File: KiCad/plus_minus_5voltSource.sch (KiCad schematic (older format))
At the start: 15 parts, among them P1 CONN_01X03, SW1 SW_Push, U1 LM7805_TO220, U2 7660, U3 LM79L05_TO92

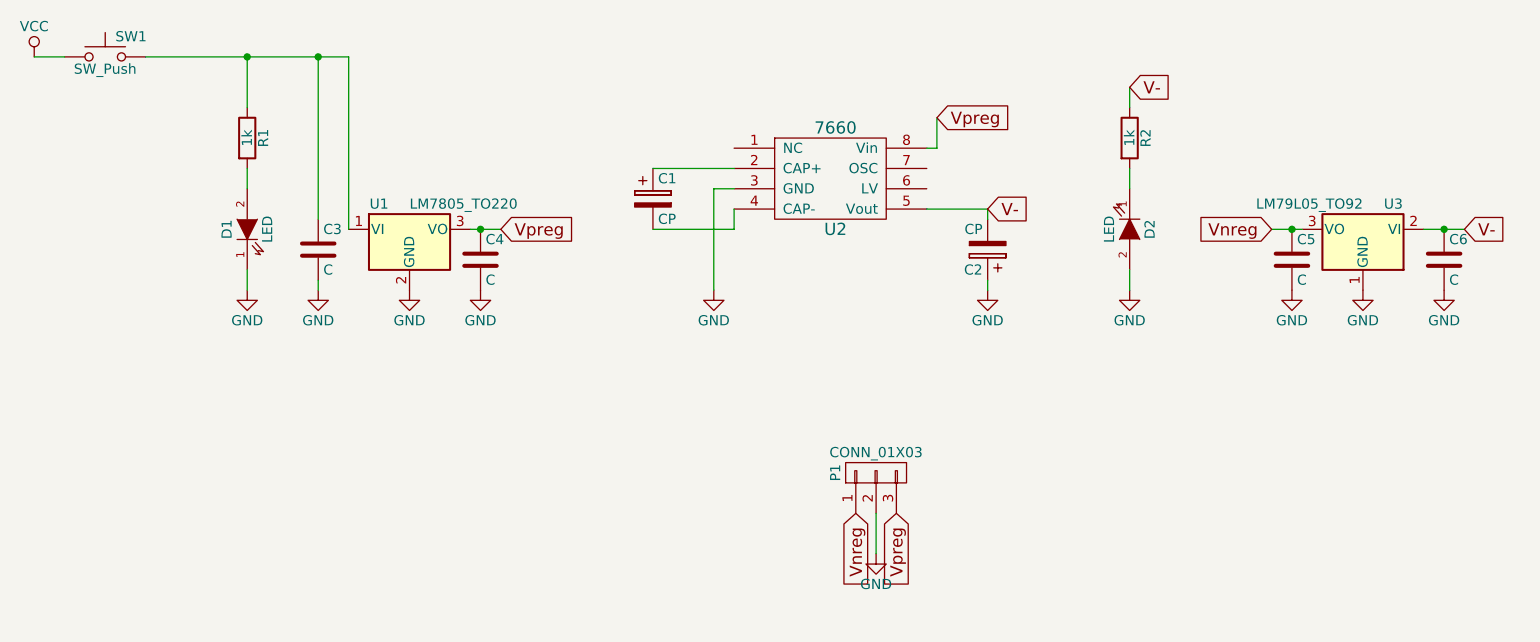
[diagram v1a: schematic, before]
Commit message: Finalized schematic by adding the usb connector for power and ground.
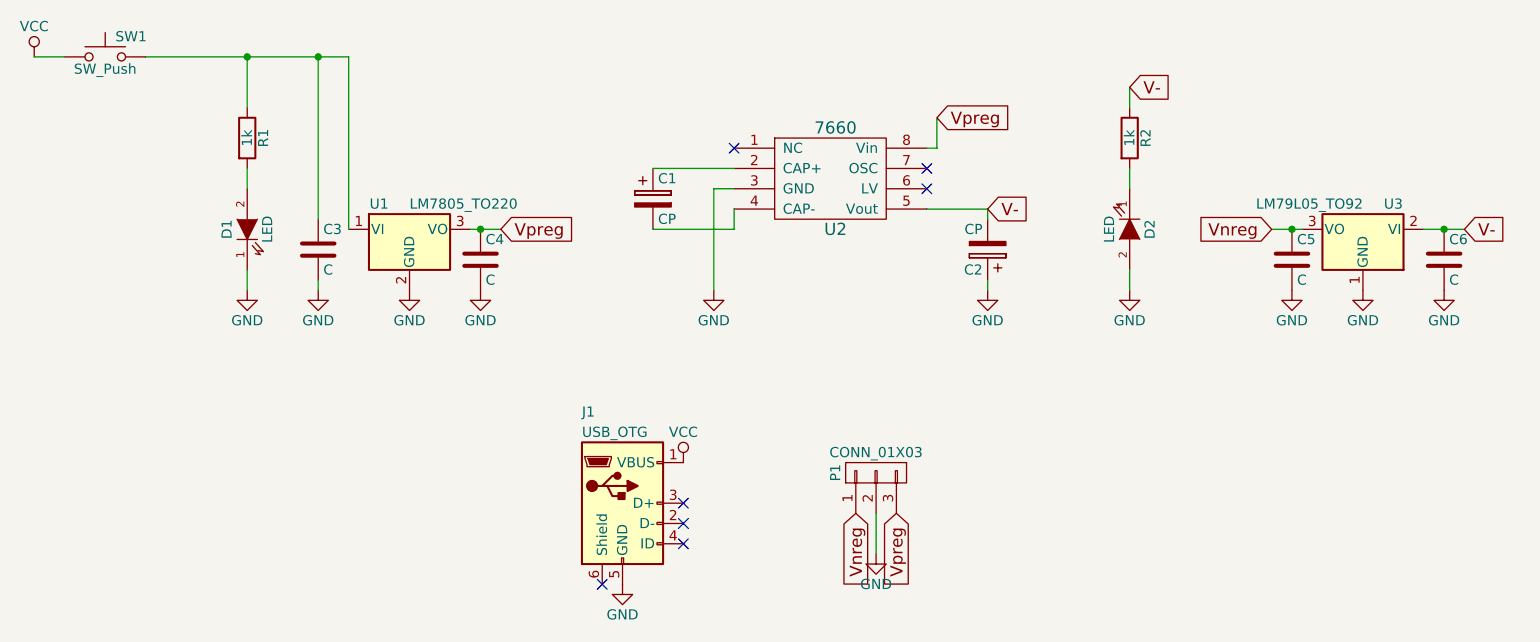
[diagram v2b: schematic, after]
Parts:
- added J1: USB_OTG, symbol USB_OTG
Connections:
- net GND: now also J1.5 (GND)
- net VCC: now also J1.1 (VBUS)
- no-connect marks 0 -> 7
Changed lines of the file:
@@
 	5550 3550 5150 3550
 $Comp
-L GND #PWR6
+L GND #PWR8
 U 1 1 55A2DE47
 P 5450 3850
-F 0 "#PWR6" H 5450 3600 50  0001 C CNN
+F 0 "#PWR8" H 5450 3600 50  0001 C CNN
 F 1 "GND" H 5450 3700 50  0000 C CNN
 F 2 "" H 5450 3850 60  0000 C CNN
@@
 	6800 3450 6500 3450
 $Comp
-L GND #PWR8
+L GND #PWR10
 U 1 1 55A2DF2E
 P 6800 3850
-F 0 "#PWR8" H 6800 3600 50  0001 C CNN
+F 0 "#PWR10" H 6800 3600 50  0001 C CNN
 F 1 "GND" H 6800 3700 50  0000 C CNN
 F 2 "" H 6800 3850 60  0000 C CNN
@@
 V-
 $Comp
-L GND #PWR7
+L GND #PWR9
 U 1 1 55A2E0F0
 P 6250 5150
-F 0 "#PWR7" H 6250 4900 50  0001 C CNN
+F 0 "#PWR9" H 6250 4900 50  0001 C CNN
 F 1 "GND" H 6250 5000 50  0000 C CNN
 F 2 "" H 6250 5150 60  0000 C CNN
@@
 $EndComp
 $Comp
-L GND #PWR9
+L GND #PWR11
 U 1 1 5796D7C9
 P 7500 3850
-F 0 "#PWR9" H 7500 3600 50  0001 C CNN
+F 0 "#PWR11" H 7500 3600 50  0001 C CNN
 F 1 "GND" H 7500 3700 50  0000 C CNN
 F 2 "" H 7500 3850 60  0000 C CNN
@@
 $EndComp
 $Comp
-L GND #PWR11
+L GND #PWR13
 U 1 1 5A2F6815
 P 8650 3850
-F 0 "#PWR11" H 8650 3600 50  0001 C CNN
+F 0 "#PWR13" H 8650 3600 50  0001 C CNN
 F 1 "GND" H 8650 3700 50  0000 C CNN
 F 2 "" H 8650 3850 60  0000 C CNN
@@
 Connection ~ 8300 3550
 $Comp
-L GND #PWR10
+L GND #PWR12
 U 1 1 5A2F7A77
 P 8300 3850
-F 0 "#PWR10" H 8300 3600 50  0001 C CNN
+F 0 "#PWR12" H 8300 3600 50  0001 C CNN
 F 1 "GND" H 8300 3700 50  0000 C CNN
 F 2 "" H 8300 3850 60  0000 C CNN
@@
 $EndComp
 $Comp
-L GND #PWR12
+L GND #PWR14
 U 1 1 5A2F7AAF
 P 9050 3850
-F 0 "#PWR12" H 9050 3600 50  0001 C CNN
+F 0 "#PWR14" H 9050 3600 50  0001 C CNN
 F 1 "GND" H 9050 3700 50  0000 C CNN
 F 2 "" H 9050 3850 60  0000 C CNN
@@
 	3500 3500 3500 2700
 Connection ~ 3500 2700
+$Comp
+L USB_OTG J1
+U 1 1 5A30A371
+P 5000 4900
+F 0 "J1" H 4800 5350 50  0000 L CNN
+F 1 "USB_OTG" H 4800 5250 50  0000 L CNN
+F 2 "" H 5150 4850 50  0001 C CNN
+F 3 "" H 5150 4850 50  0001 C CNN
+	1    5000 4900
+	1    0    0    -1
+$EndComp
+$Comp
+L GND #PWR6
+U 1 1 5A30A705
+P 5000 5300
+F 0 "#PWR6" H 5000 5050 50  0001 C CNN
+F 1 "GND" H 5000 5150 50  0000 C CNN
+F 2 "" H 5000 5300 60  0000 C CNN
+F 3 "" H 5000 5300 60  0000 C CNN
+	1    5000 5300
+	1    0    0    -1
+$EndComp
+$Comp
+L VCC #PWR7
+U 1 1 5A30A740
+P 5300 4700
+F 0 "#PWR7" H 5300 4550 50  0001 C CNN
+F 1 "VCC" H 5300 4850 50  0000 C CNN
+F 2 "" H 5300 4700 60  0000 C CNN
+F 3 "" H 5300 4700 60  0000 C CNN
+	1    5300 4700
+	1    0    0    -1
+$EndComp
+NoConn ~ 5300 4900
+NoConn ~ 5300 5000
+NoConn ~ 5300 5100
+NoConn ~ 4900 5300
+NoConn ~ 6500 3250
+NoConn ~ 6500 3350
+NoConn ~ 5550 3150
 $EndSCHEMATC

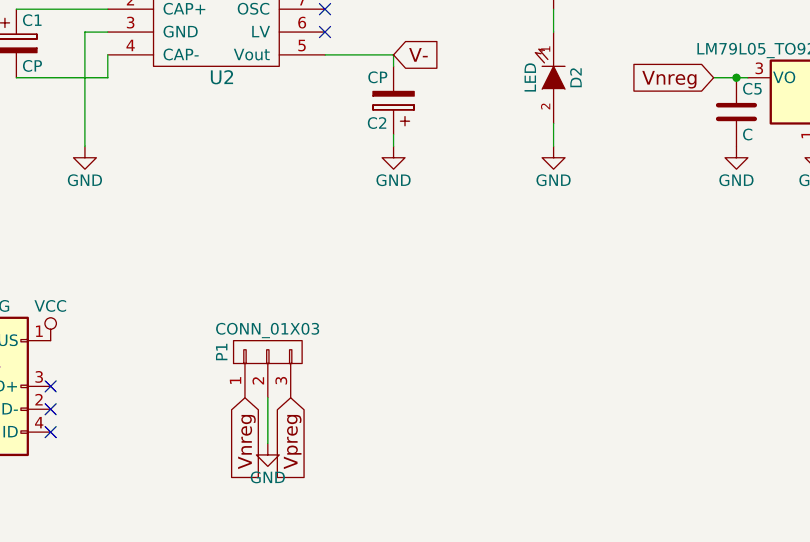
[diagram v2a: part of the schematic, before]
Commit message: Formatted BOM.
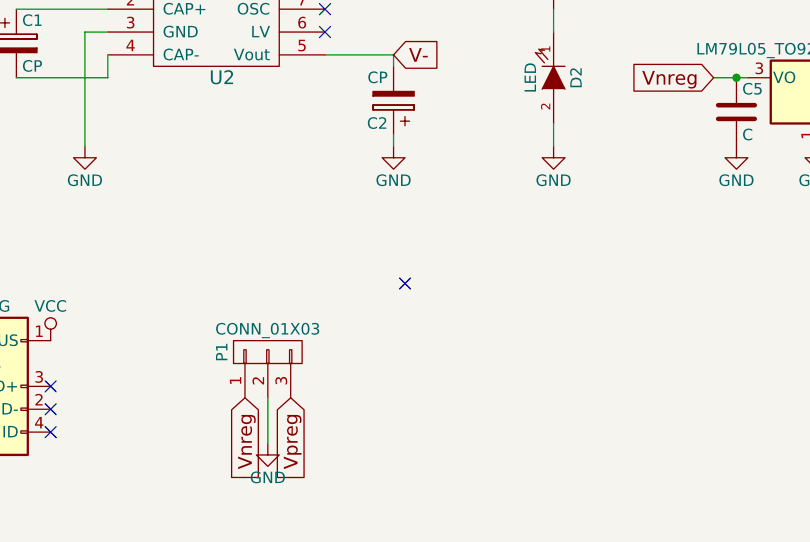
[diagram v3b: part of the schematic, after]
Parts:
- C1, C2: footprint Capacitors_ThroughHole:C_Radial_D5_L6_P2.5 -> Capacitors_ThroughHole:CP_Radial_D5.0mm_P2.50mm
- C3, C4, C5, C6: footprint (none) -> Capacitors_ThroughHole:C_Disc_D3.0mm_W2.0mm_P2.50mm
- D1, D2: footprint LEDs:LED_0805 -> LEDs:LED_D3.0mm
- J1: footprint (none) -> Connect:USB_Micro-B
- P1: footprint Pin_Headers:Pin_Header_Angled_1x03 -> Pin_Headers:Pin_Header_Angled_1x03_Pitch2.54mm
- R1, R2: footprint Resistors_SMD:R_0805_HandSoldering -> Resistors_ThroughHole:R_Axial_DIN0204_L3.6mm_D1.6mm_P5.08mm_Vertical
- SW1: footprint (none) -> Buttons_Switches_ThroughHole:SW_PUSH_6mm
- U1: footprint TO_SOT_Packages_THT:TO-220_Vertical -> TO_SOT_Packages_THT:TO-92_Inline_Narrow_Oval
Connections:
- no-connect marks 7 -> 8
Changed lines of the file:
@@
 F 0 "C1" H 5175 3500 50  0000 L CNN
 F 1 "CP" H 5175 3300 50  0000 L CNN
-F 2 "Capacitors_ThroughHole:C_Radial_D5_L6_P2.5" H 5188 3250 30  0001 C CNN
+F 2 "Capacitors_ThroughHole:CP_Radial_D5.0mm_P2.50mm" H 5188 3250 30  0001 C CNN
 F 3 "" H 5150 3400 60  0000 C CNN
 	1    5150 3400
@@
 F 0 "C2" H 6825 3750 50  0000 L CNN
 F 1 "CP" H 6825 3550 50  0000 L CNN
-F 2 "Capacitors_ThroughHole:C_Radial_D5_L6_P2.5" H 6838 3500 30  0001 C CNN
+F 2 "Capacitors_ThroughHole:CP_Radial_D5.0mm_P2.50mm" H 6838 3500 30  0001 C CNN
 F 3 "" H 6800 3650 60  0000 C CNN
 	1    6800 3650
@@
 	5550 3550 5150 3550
 $Comp
-L GND #PWR8
+L GND #PWR01
 U 1 1 55A2DE47
 P 5450 3850
-F 0 "#PWR8" H 5450 3600 50  0001 C CNN
+F 0 "#PWR01" H 5450 3600 50  0001 C CNN
 F 1 "GND" H 5450 3700 50  0000 C CNN
 F 2 "" H 5450 3850 60  0000 C CNN
@@
 	6800 3450 6500 3450
 $Comp
-L GND #PWR10
+L GND #PWR02
 U 1 1 55A2DF2E
 P 6800 3850
-F 0 "#PWR10" H 6800 3600 50  0001 C CNN
+F 0 "#PWR02" H 6800 3600 50  0001 C CNN
 F 1 "GND" H 6800 3700 50  0000 C CNN
 F 2 "" H 6800 3850 60  0000 C CNN
@@
 V-
 $Comp
-L GND #PWR9
+L GND #PWR03
 U 1 1 55A2E0F0
 P 6250 5150
-F 0 "#PWR9" H 6250 4900 50  0001 C CNN
+F 0 "#PWR03" H 6250 4900 50  0001 C CNN
 F 1 "GND" H 6250 5000 50  0000 C CNN
 F 2 "" H 6250 5150 60  0000 C CNN
@@
 F 0 "D1" H 3150 3650 50  0000 C CNN
 F 1 "LED" H 3150 3450 50  0000 C CNN
-F 2 "LEDs:LED_0805" H 3150 3550 60  0001 C CNN
+F 2 "LEDs:LED_D3.0mm" H 3150 3550 60  0001 C CNN
 F 3 "" H 3150 3550 60  0000 C CNN
 	1    3150 3550
@@
 F 0 "R1" V 3230 3100 50  0000 C CNN
 F 1 "1k" V 3150 3100 50  0000 C CNN
-F 2 "Resistors_SMD:R_0805_HandSoldering" V 3080 3100 30  0001 C CNN
+F 2 "Resistors_ThroughHole:R_Axial_DIN0204_L3.6mm_D1.6mm_P5.08mm_Vertical" V 3080 3100 30  0001 C CNN
 F 3 "" H 3150 3100 30  0000 C CNN
 	1    3150 3100
@@
 $EndComp
 $Comp
-L VCC #PWR1
+L VCC #PWR04
 U 1 1 560AE1BD
 P 2100 2700
-F 0 "#PWR1" H 2100 2550 50  0001 C CNN
+F 0 "#PWR04" H 2100 2550 50  0001 C CNN
 F 1 "VCC" H 2100 2850 50  0000 C CNN
 F 2 "" H 2100 2700 60  0000 C CNN
@@
 $EndComp
 $Comp
-L GND #PWR2
+L GND #PWR05
 U 1 1 560AE1E0
 P 3150 3850
-F 0 "#PWR2" H 3150 3600 50  0001 C CNN
+F 0 "#PWR05" H 3150 3600 50  0001 C CNN
 F 1 "GND" H 3150 3700 50  0000 C CNN
 F 2 "" H 3150 3850 60  0000 C CNN
@@
 F 0 "P1" H 6250 4950 50  0000 C CNN
 F 1 "CONN_01X03" V 6350 4750 50  0000 C CNN
-F 2 "Pin_Headers:Pin_Header_Angled_1x03" H 6250 4750 60  0001 C CNN
+F 2 "Pin_Headers:Pin_Header_Angled_1x03_Pitch2.54mm" H 6250 4750 60  0001 C CNN
 F 3 "" H 6250 4750 60  0000 C CNN
 	1    6250 4750
@@
 F 0 "R2" V 7580 3100 50  0000 C CNN
 F 1 "1k" V 7500 3100 50  0000 C CNN
-F 2 "Resistors_SMD:R_0805_HandSoldering" V 7430 3100 30  0001 C CNN
+F 2 "Resistors_ThroughHole:R_Axial_DIN0204_L3.6mm_D1.6mm_P5.08mm_Vertical" V 7430 3100 30  0001 C CNN
 F 3 "" H 7500 3100 30  0000 C CNN
 	1    7500 3100
@@
 $EndComp
 $Comp
-L GND #PWR11
+L GND #PWR06
 U 1 1 5796D7C9
 P 7500 3850
-F 0 "#PWR11" H 7500 3600 50  0001 C CNN
+F 0 "#PWR06" H 7500 3600 50  0001 C CNN
 F 1 "GND" H 7500 3700 50  0000 C CNN
 F 2 "" H 7500 3850 60  0000 C CNN
@@
 F 0 "D2" H 7500 3650 50  0000 C CNN
 F 1 "LED" H 7500 3450 50  0000 C CNN
-F 2 "LEDs:LED_0805" H 7500 3550 60  0001 C CNN
+F 2 "LEDs:LED_D3.0mm" H 7500 3550 60  0001 C CNN
 F 3 "" H 7500 3550 60  0000 C CNN
 	1    7500 3550
@@
 F 0 "SW1" H 2500 2800 50  0000 L CNN
 F 1 "SW_Push" H 2450 2640 50  0000 C CNN
-F 2 "" H 2450 2900 50  0001 C CNN
+F 2 "Buttons_Switches_ThroughHole:SW_PUSH_6mm" H 2450 2900 50  0001 C CNN
 F 3 "" H 2450 2900 50  0001 C CNN
 	1    2450 2700
@@
 $EndComp
 $Comp
-L GND #PWR13
+L GND #PWR07
 U 1 1 5A2F6815
 P 8650 3850
-F 0 "#PWR13" H 8650 3600 50  0001 C CNN
+F 0 "#PWR07" H 8650 3600 50  0001 C CNN
 F 1 "GND" H 8650 3700 50  0000 C CNN
 F 2 "" H 8650 3850 60  0000 C CNN
@@
 F 0 "U1" H 3800 3675 50  0000 C CNN
 F 1 "LM7805_TO220" H 3950 3675 50  0000 L CNN
-F 2 "TO_SOT_Packages_THT:TO-220_Vertical" H 3950 3775 50  0001 C CIN
+F 2 "TO_SOT_Packages_THT:TO-92_Inline_Narrow_Oval" H 3950 3775 50  0001 C CIN
 F 3 "" H 3950 3500 50  0001 C CNN
 	1    3950 3550
@@
 V-
 $Comp
-L GND #PWR4
+L GND #PWR08
 U 1 1 5A2F6F94
 P 3950 3850
-F 0 "#PWR4" H 3950 3600 50  0001 C CNN
+F 0 "#PWR08" H 3950 3600 50  0001 C CNN
 F 1 "GND" H 3950 3700 50  0000 C CNN
 F 2 "" H 3950 3850 60  0000 C CNN
@@
 F 0 "C3" H 3525 3750 50  0000 L CNN
 F 1 "C" H 3525 3550 50  0000 L CNN
-F 2 "" H 3538 3500 50  0001 C CNN
+F 2 "Capacitors_ThroughHole:C_Disc_D3.0mm_W2.0mm_P2.50mm" H 3538 3500 50  0001 C CNN
 F 3 "" H 3500 3650 50  0001 C CNN
 	1    3500 3650
@@
 F 0 "C4" H 4325 3800 50  0000 L CNN
 F 1 "C" H 4325 3600 50  0000 L CNN
-F 2 "" H 4338 3550 50  0001 C CNN
+F 2 "Capacitors_ThroughHole:C_Disc_D3.0mm_W2.0mm_P2.50mm" H 4338 3550 50  0001 C CNN
 F 3 "" H 4300 3700 50  0001 C CNN
 	1    4300 3700
@@
 F 0 "C5" H 8325 3800 50  0000 L CNN
 F 1 "C" H 8325 3600 50  0000 L CNN
-F 2 "" H 8338 3550 50  0001 C CNN
+F 2 "Capacitors_ThroughHole:C_Disc_D3.0mm_W2.0mm_P2.50mm" H 8338 3550 50  0001 C CNN
 F 3 "" H 8300 3700 50  0001 C CNN
 	1    8300 3700
@@
 F 0 "C6" H 9075 3800 50  0000 L CNN
 F 1 "C" H 9075 3600 50  0000 L CNN
-F 2 "" H 9088 3550 50  0001 C CNN
+F 2 "Capacitors_ThroughHole:C_Disc_D3.0mm_W2.0mm_P2.50mm" H 9088 3550 50  0001 C CNN
 F 3 "" H 9050 3700 50  0001 C CNN
 	1    9050 3700
@@
 Connection ~ 8300 3550
 $Comp
-L GND #PWR12
+L GND #PWR09
 U 1 1 5A2F7A77
 P 8300 3850
-F 0 "#PWR12" H 8300 3600 50  0001 C CNN
+F 0 "#PWR09" H 8300 3600 50  0001 C CNN
 F 1 "GND" H 8300 3700 50  0000 C CNN
 F 2 "" H 8300 3850 60  0000 C CNN
@@
 $EndComp
 $Comp
-L GND #PWR14
+L GND #PWR010
 U 1 1 5A2F7AAF
 P 9050 3850
-F 0 "#PWR14" H 9050 3600 50  0001 C CNN
+F 0 "#PWR010" H 9050 3600 50  0001 C CNN
 F 1 "GND" H 9050 3700 50  0000 C CNN
 F 2 "" H 9050 3850 60  0000 C CNN
@@
 $EndComp
 $Comp
-L GND #PWR5
+L GND #PWR011
 U 1 1 5A2F7BF5
 P 4300 3850
-F 0 "#PWR5" H 4300 3600 50  0001 C CNN
+F 0 "#PWR011" H 4300 3600 50  0001 C CNN
 F 1 "GND" H 4300 3700 50  0000 C CNN
 F 2 "" H 4300 3850 60  0000 C CNN
@@
 $EndComp
 $Comp
-L GND #PWR3
+L GND #PWR012
 U 1 1 5A2F7C2D
 P 3500 3850
-F 0 "#PWR3" H 3500 3600 50  0001 C CNN
+F 0 "#PWR012" H 3500 3600 50  0001 C CNN
 F 1 "GND" H 3500 3700 50  0000 C CNN
 F 2 "" H 3500 3850 60  0000 C CNN
@@
 F 0 "J1" H 4800 5350 50  0000 L CNN
 F 1 "USB_OTG" H 4800 5250 50  0000 L CNN
-F 2 "" H 5150 4850 50  0001 C CNN
+F 2 "Connect:USB_Micro-B" H 5150 4850 50  0001 C CNN
 F 3 "" H 5150 4850 50  0001 C CNN
 	1    5000 4900
@@
 $EndComp
 $Comp
-L GND #PWR6
+L GND #PWR013
 U 1 1 5A30A705
 P 5000 5300
-F 0 "#PWR6" H 5000 5050 50  0001 C CNN
+F 0 "#PWR013" H 5000 5050 50  0001 C CNN
 F 1 "GND" H 5000 5150 50  0000 C CNN
 F 2 "" H 5000 5300 60  0000 C CNN
@@
 $EndComp
 $Comp
-L VCC #PWR7
+L VCC #PWR014
 U 1 1 5A30A740
 P 5300 4700
-F 0 "#PWR7" H 5300 4550 50  0001 C CNN
+F 0 "#PWR014" H 5300 4550 50  0001 C CNN
 F 1 "VCC" H 5300 4850 50  0000 C CNN
 F 2 "" H 5300 4700 60  0000 C CNN
@@
 NoConn ~ 6500 3350
 NoConn ~ 5550 3150
+NoConn ~ 6850 4450
 $EndSCHEMATC

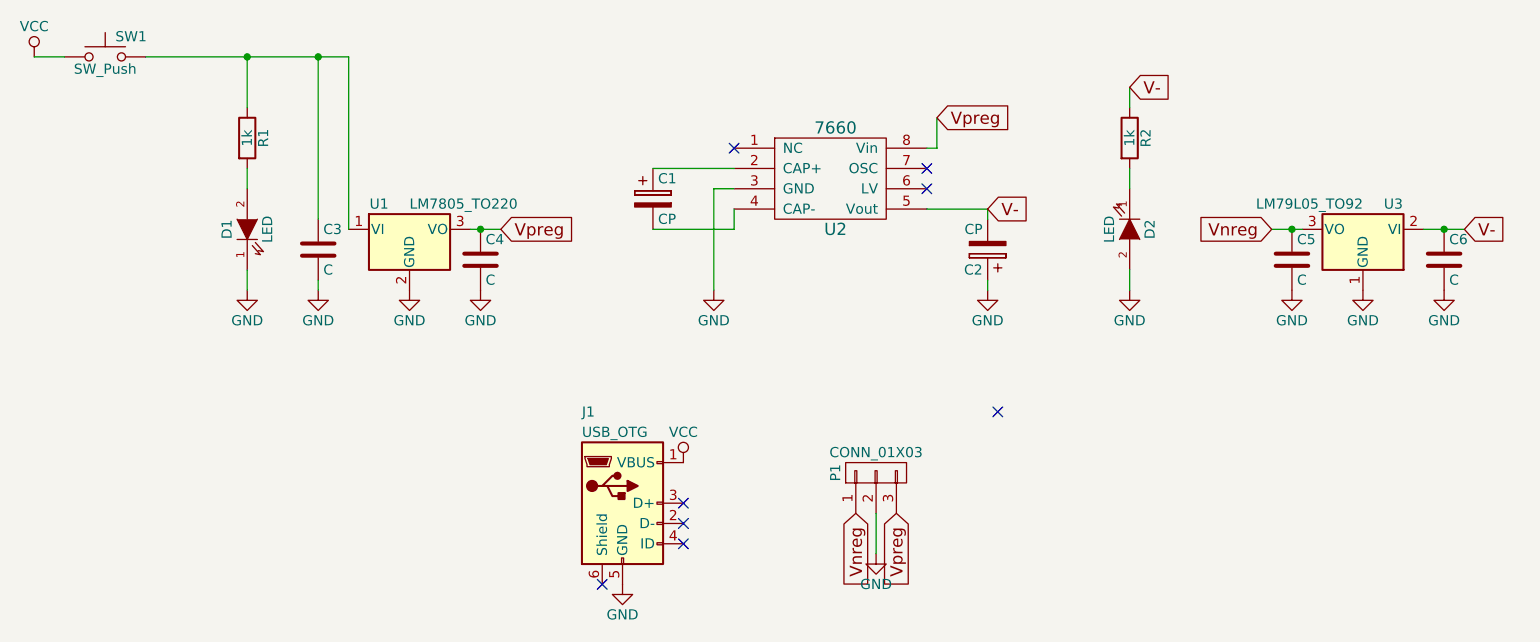
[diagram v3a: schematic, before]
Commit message: Edited voltage regulator part numbers to reflect actual part numbers. Added a schmatic folder with schematic pdf.
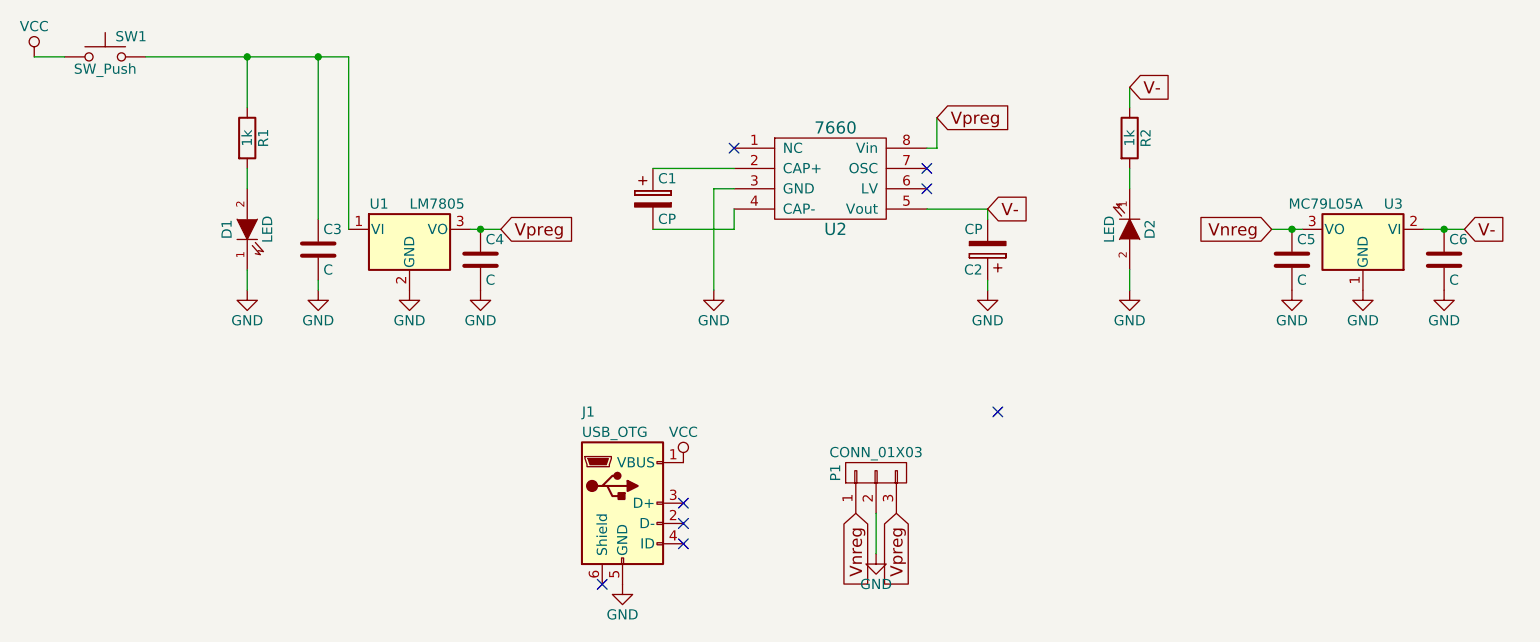
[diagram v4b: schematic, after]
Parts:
- U1: value LM7805_TO220 -> LM7805
- U3: value LM79L05_TO92 -> MC79L05A
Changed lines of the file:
@@
 encoding utf-8
 Sheet 1 1
-Title "+/-5V Portable supply"
+Title "Orion"
 Date "2017-12-11"
 Rev "2.0.0"
-Comp "AVO Labs"
+Comp "AVO Electronics"
 Comment1 "Cameron Belt"
-Comment2 ""
+Comment2 "+/-5V Portable supply"
 Comment3 ""
 Comment4 ""
@@
 P 8650 3550
 F 0 "U3" H 8500 3425 50  0000 C CNN
-F 1 "LM79L05_TO92" H 8650 3425 50  0000 L CNN
+F 1 "MC79L05A" H 8650 3425 50  0000 L CNN
 F 2 "TO_SOT_Packages_THT:TO-92_Inline_Narrow_Oval" H 8650 3350 50  0001 C CIN
 F 3 "" H 8650 3550 50  0001 C CNN
@@
 P 3950 3550
 F 0 "U1" H 3800 3675 50  0000 C CNN
-F 1 "LM7805_TO220" H 3950 3675 50  0000 L CNN
+F 1 "LM7805" H 3950 3675 50  0000 L CNN
 F 2 "TO_SOT_Packages_THT:TO-92_Inline_Narrow_Oval" H 3950 3775 50  0001 C CIN
 F 3 "" H 3950 3500 50  0001 C CNN
